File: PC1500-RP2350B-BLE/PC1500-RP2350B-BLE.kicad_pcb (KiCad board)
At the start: 2 copper layers, 31.8 x 43 mm, 71 parts, among them J1 SD_Card_Device, J2 USB_C_Receptacle_USB2.0_14P, J3 40-Pin Connector, J4 SWD_DEBUG, J5 SPARE_GPIO_U1, J6 SPARE_GPIO_U9, SW1 BOOTSEL, U1 RP2350B, U10 TCA9406DC, U2 AS6C62256-55SIN, U3 SLG46826G, U4 AP2112K-3.3, U5 W25Q32JVSS, U6 TXS0108EPW, U8 RN4871, U9 SLG46826G, X1 Crystal

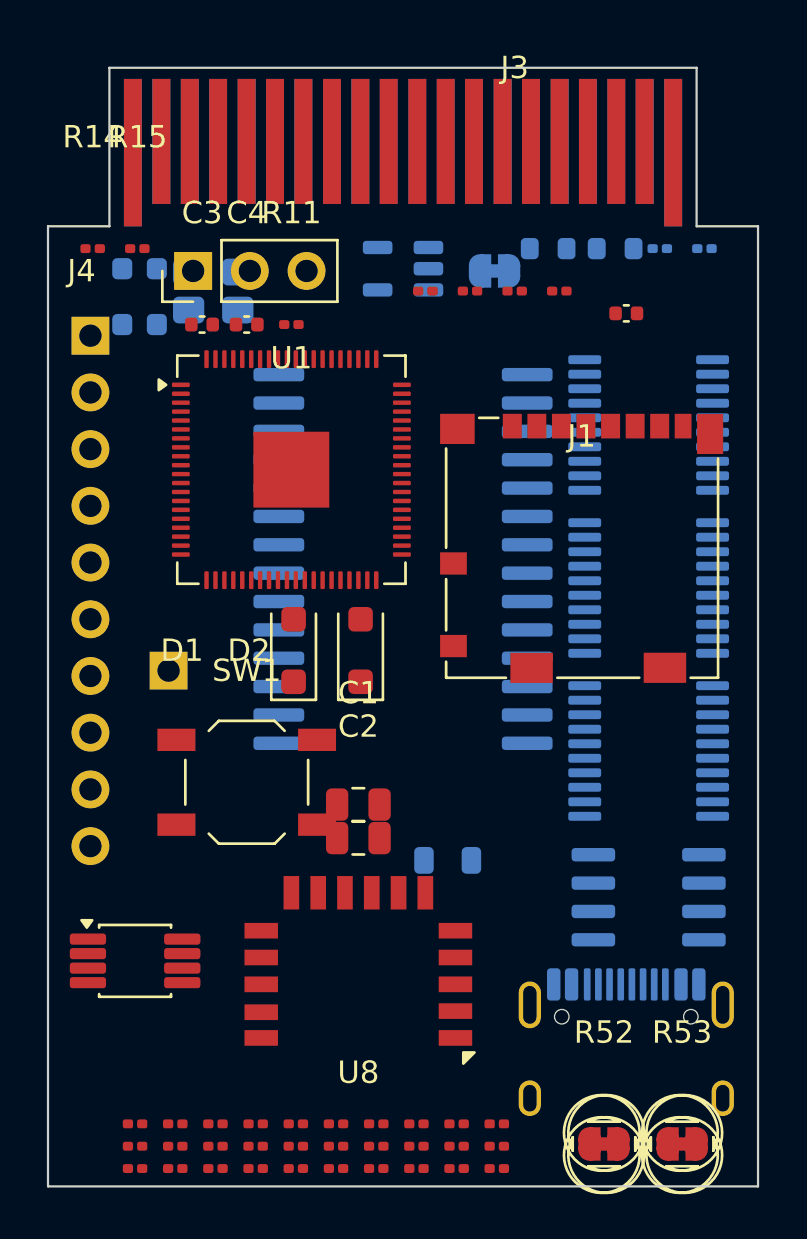
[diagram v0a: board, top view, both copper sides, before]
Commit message: Add GreenPak bench-test/provisioning tools and no-level-shifters board variants
- GreenPakTester: standalone Pico 2 W bench-test firmware for the
  GreenPAK SLG46826V, with a VS-Code-extension-friendly project layout
  (Run/Flash/Serial-Monitor buttons via the Raspberry Pi Pico extension).
- GreenPak_Provision: standalone GreenPAK NVM provisioner, split out of
  RP2350's multi-target CMakeLists.txt into its own extension-friendly
  project for the same easy build/flash/serial-monitor workflow.
- PC1500-Pico2W-Dongle and PC1500-RP2350B-BLE: latest schematic/PCB
  edits, plus a new no-level-shifters KiCad variant of each board.
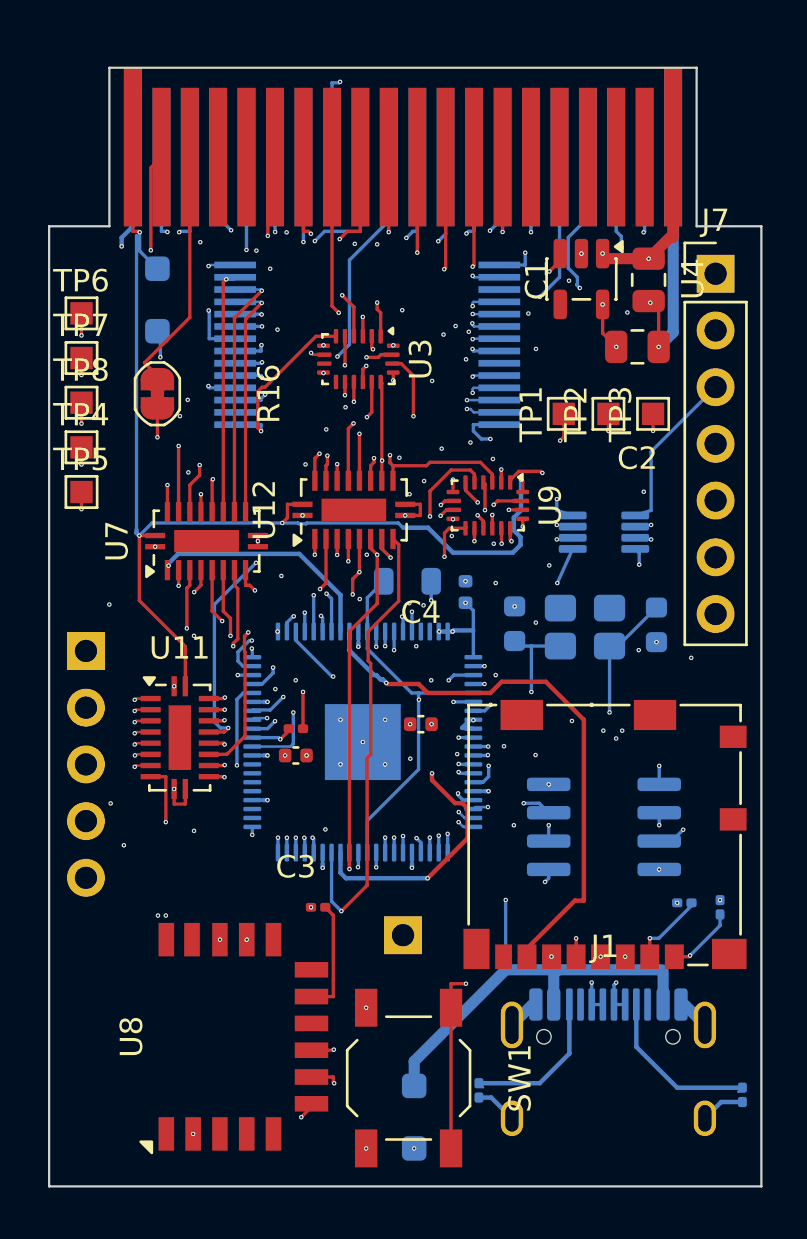
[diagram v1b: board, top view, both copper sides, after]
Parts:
- removed J4: SWD_DEBUG, Connector_PinHeader_2.54mm:PinHeader_1x03_P2.54mm_Vertical
- removed R1, R2: 220k, Resistor_SMD:R_0603_1608Metric
- removed R15, R19, R20: 10K, Resistor_SMD:R_0201_0603Metric
- removed R22, R24, R26, R28, R30, R32, R34, R36, R38, R40, R42, R44, R46, R48, R50: 4.7k, Resistor_SMD:R_0201_0603Metric
- removed R23, R25, R27, R29, R31, R33, R35, R37, R39, R41, R43, R45, R47, R49, R51: 10k, Resistor_SMD:R_0201_0603Metric
- removed R52, R53: Jumper_2_Bridged, Jumper:SolderJumper-2_P1.3mm_Bridged_RoundedPad1.0x1.5mm
- removed U6: TXS0108EPW, Package_SO:TSSOP-20_4.4x6.5mm_P0.65mm
- added J7: SWD_I2C_HEADER, Connector_PinHeader_2.54mm:PinHeader_1x07_P2.54mm_Vertical, F.Cu at (164.0, 59.2)
- added TP1: TRIG_RD, TestPoint:TestPoint_Pad_1.0x1.0mm, F.Cu at (157.2, 65.5)
- added TP2: AD15_MCU, TestPoint:TestPoint_Pad_1.0x1.0mm, F.Cu at (159.2, 65.5)
- added TP3: AD13_MCU, TestPoint:TestPoint_Pad_1.0x1.0mm, F.Cu at (161.2, 65.5)
- added TP4: GPIO19, TestPoint:TestPoint_Pad_1.0x1.0mm, F.Cu at (135.6, 67.0)
- added TP5: GPIO20, TestPoint:TestPoint_Pad_1.0x1.0mm, F.Cu at (135.6, 69.0)
- added TP6: GPIO44, TestPoint:TestPoint_Pad_1.0x1.0mm, F.Cu at (135.6, 61.0)
- added TP7: GPIO45, TestPoint:TestPoint_Pad_1.0x1.0mm, F.Cu at (135.6, 63.0)
- added TP8: GPIO34, TestPoint:TestPoint_Pad_1.0x1.0mm, F.Cu at (135.6, 65.0)
- added U11: FXMA108, Package_DFN_QFN:WQFN-20-1EP_2.5x4.5mm_P0.5mm_EP1x2.9mm, F.Cu at (140.0, 80.0)
- added U12: FXMA108, Package_DFN_QFN:WQFN-20-1EP_2.5x4.5mm_P0.5mm_EP1x2.9mm, F.Cu at (147.8, 69.8)
- added U7: FXMA108, Package_DFN_QFN:WQFN-20-1EP_2.5x4.5mm_P0.5mm_EP1x2.9mm, F.Cu at (141.2, 71.2)
- C12, C13: value C -> 15pF
- C14, R17, R18, U1: moved to B.Cu
- C3, C4: value C -> 100nF
- D1, D2: value D_Schottky -> PMEG6010ELR; moved to B.Cu
- J1: value SD_Card_Device -> microSD
- J2: value USB_C_Receptacle_USB2.0_14P -> USB-C (programming/debug)
- J3: value 40-Pin Connector -> PC-1500 40-pin cartridge slot
- J5: value SPARE_GPIO_U1 -> PC1500_SENSE_JUMPER; footprint Connector_PinHeader_2.54mm:PinHeader_1x10_P2.54mm_Vertical -> Connector_PinHeader_2.54mm:PinHeader_1x05_P2.54mm_Vertical
- L2: value L -> 1uH
- R11: value R -> 1K
- R16, U4: moved to F.Cu
- U10: value TCA9406DC -> TCA9406DCUR; footprint Package_SO:VSSOP-8_3x3mm_P0.65mm -> Package_SO:VSSOP-8_2.3x2mm_P0.5mm; moved to B.Cu
- U2: value AS6C62256-55SIN -> AS6C62256-55STCN; footprint Package_SO:SOP-28_8.4x18.16mm_P1.27mm -> Sharp-PC-Footprints:AS6C62256_STSOP-28_11.8x8mm_P0.55mm
- U3, U9: value SLG46826G -> SLG46826V; footprint Package_SO:TSSOP-20_4.4x6.5mm_P0.65mm -> Package_DFN_QFN:Renesas_UQFN-20_2x3mm_P0.4mm_LayoutBorder4x6y; moved to F.Cu
- U5: value W25Q32JVSS -> W25Q32RVXHJQ
- X1: value Crystal -> 12MHz (Abracon ABM8-272-T3)
- moved R10 39.0 mm to (153.4, 95.8), turned to -90 degrees
- moved R9 38.1 mm to (165.2, 96.0), turned to -90 degrees
- moved R14 31.2 mm to (146.2, 87.6)
- moved R17 30.6 mm to (164.2, 87.6), turned to -90 degrees
- moved R18 29.0 mm to (162.6, 87.4)
- moved U10 28.5 mm to (159.0, 70.8), turned to 180 degrees
- moved C12 28.1 mm to (161.3, 75.0), turned to -90 degrees
- moved C1 26.9 mm to (161.0, 59.5), turned to 90 degrees
- moved C2 25.3 mm to (160.5, 62.5), turned to 180 degrees
- moved X1 22.4 mm to (158.2, 75.0)
- moved C13 21.5 mm to (155.0, 74.9), turned to 90 degrees
- moved D2 21.0 mm to (150.5, 97.0)
- moved C3 19.8 mm to (145.2, 80.8), turned to 180 degrees
- moved C4 19.5 mm to (150.8, 79.4)
- moved R11 18.1 mm to (145.2, 79.6)
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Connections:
- J1 pad 8: unconnected-(J1-DAT1-Pad8) -> DAT1
- J1 pad 9: unconnected-(J1-DAT2-Pad9) -> DAT2
- J2 pad A1: Net-(J2-GND-PadA1) -> GND
- J2 pad A12: Net-(J2-GND-PadA1) -> GND
- J2 pad A4: Net-(J2-VBUS-PadA4) -> VBUS
- J2 pad A5: unconnected-(J2-CC1-PadA5) -> CC1_R
- J2 pad A9: Net-(J2-VBUS-PadA4) -> VBUS
- J2 pad B1: Net-(J2-GND-PadA1) -> GND
- J2 pad B12: Net-(J2-GND-PadA1) -> GND
- J2 pad B4: Net-(J2-VBUS-PadA4) -> VBUS
- J2 pad B5: unconnected-(J2-CC2-PadB5) -> CC2_R
- J2 pad B6: unconnected-(J2-D+-PadB6) -> USB_DP
- J2 pad B7: unconnected-(J2-D--PadB7) -> USB_DM
- J2 pad B9: Net-(J2-VBUS-PadA4) -> VBUS
- J2 pad SH: unconnected-(J2-SHIELD-PadSH) -> GND
- J3 pad 5: S4 -> unconnected-(J3-Pin_5-Pad5)
- J5 pad 1: GPIO31 -> PC1500_SENSE
- J5 pad 2: GPIO35 -> GND
- J5 pad 3: GPIO36 -> GND
- J5 pad 4: GPIO37 -> VGG
- J5 pad 5: GPIO38 -> +3V3
- J6 pad 1: GREENPAK2_IO13 -> GREENPAK2_IO14
- R11 pad 1: +3V3 -> XOUT_MCU
- R11 pad 2: unconnected-(R11-Pad2) -> XOUT
- R16 pad 2: GREENPAK2_IO14 -> GREENPAK2_IO13
- U1 pad 12: DATA0_MCU -> AD13_MCU
- U1 pad 13: DATA1_MCU -> AD14_MCU
- U1 pad 14: DATA2_MCU -> AD15_MCU
- U1 pad 16: DATA3_MCU -> DATA2_MCU
- U1 pad 17: DATA4_MCU -> DATA1_MCU
- U1 pad 18: DATA5_MCU -> DATA0_MCU
- U1 pad 19: DATA6_MCU -> GPIO19
- U1 pad 20: DATA7_MCU -> GPIO20
- U1 pad 21: TRIG_RD_MCU -> BLE_WAKE
- U1 pad 22: TRIG_WR_MCU -> GPIO22
- U1 pad 23: GREENPAK1_SDA -> GPIO23
- U1 pad 25: GREENPAK1_SCL -> GPIO24
- U1 pad 26: (no net) -> GPIO25
- U1 pad 27: (no net) -> GPIO26
- U1 pad 28: ROM_SRAM_STATUS -> unconnected-(U1-GPIO27-Pad28)
- U1 pad 31: XOUT -> XOUT_MCU
- U1 pad 36: AD13 -> GREENPAK1_SDA
- U1 pad 37: AD14 -> GREENPAK1_SCL
- U1 pad 38: AD15 -> TRIG_RD
- U1 pad 39: GPIO31 -> TRIG_WR
- U1 pad 43: BLE_WAKE -> GPIO34
- U1 pad 44: GPIO35 -> DATA3_MCU
- U1 pad 45: GPIO36 -> DATA4_MCU
- U1 pad 46: GPIO37 -> DATA5_MCU
- U1 pad 47: GPIO38 -> DATA6_MCU
- U1 pad 48: GPIO39 -> DATA7_MCU
- U1 pad 65: unconnected-(U1-VREG_FB-Pad65) -> DVDD
- U2 pad 17: D5 -> unconnected-(U2-Q5-Pad17)
- U3 pad 1: ROM_SRAM_STATUS -> DME0
- U3 pad 11: SRAM_A11 -> unconnected-(U3-IO6-Pad11)
- U3 pad 2: S4 -> PC1500_SENSE
- U3 pad 3: PRE_DME0_CS -> SRAM_CS
- U3 pad 9: SRAM_A12 -> unconnected-(U3-IO7-Pad9)
- U9 pad 1: GREENPAK2_IO14 -> TRIG_RD
- U9 pad 11: TRIG_RD -> Net-(U9-IO6)
- U9 pad 15: AD15 -> Net-(U9-IO4)
- U9 pad 17: AD13 -> PV
- U9 pad 18: AD12 -> OD
- U9 pad 19: AD11 -> DME0
- U9 pad 20: VGG -> VCC
- U9 pad 3: PRE_DME0_CS -> AD15
- U9 pad 4: PV -> AD14_MCU
- U9 pad 5: SRAM_CS -> AD13_MCU
- U9 pad 6: OD -> AD12_MCU
- U9 pad 7: VGG -> +3V3
- U9 pad 8: DME0 -> AD11_MCU
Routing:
- net VBUS: track 0.00 -> 63.2 mm, vias 0 -> 4
- net VCC: track 0.00 -> 62.1 mm, vias 0 -> 5
- net AD2: track 0.00 -> 46.9 mm, vias 0 -> 5
- net AD14: track 0.00 -> 44.6 mm, vias 0 -> 6
- net AD1: track 0.00 -> 44.2 mm, vias 0 -> 3
- net AD0: track 0.00 -> 41.4 mm, vias 0 -> 3
- net AD3: track 0.00 -> 38.9 mm, vias 0 -> 5
- net AD5: track 0.00 -> 38.1 mm, vias 0 -> 4
- net AD6: track 0.00 -> 37.6 mm, vias 0 -> 4
- net AD4: track 0.00 -> 37.5 mm, vias 0 -> 4
- net AD7: track 0.00 -> 37.4 mm, vias 0 -> 4
- net PV: track 0.00 -> 36.8 mm, vias 0 -> 5
- net AD9: track 0.00 -> 33.0 mm, vias 0 -> 4
- net D7: track 0.00 -> 32.5 mm, vias 0 -> 5
- net D3: track 0.00 -> 32.2 mm, vias 0 -> 4
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- added copper zone on In4.Cu, net +3V3
- added copper zone on In1.Cu, net GND
- added copper zone on In5.Cu, net VGG
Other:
- board size 31.8 x 43 mm -> 31.9 x 43 mm
- copper layers 2 -> 8
